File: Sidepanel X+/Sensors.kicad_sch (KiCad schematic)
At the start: 8 parts, among them IC1 TMP112AQDRLRQ1, U1 GUVA-C32SM

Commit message: fix for the issues: #19, #18 moved some components from the edge away to avoid collisions with the new structure
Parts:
- U1: footprint Package_SO:SO-4_4.4x3.6mm_P2.54mm -> STS_UV:OLGA 2mm x 2,3mm
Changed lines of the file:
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@@
     (property "Reference" "U1" (id 0) (at 60.96 34.29 0))
     (property "Value" "GUVA-C32SM" (id 1) (at 60.96 36.83 0))
-    (property "Footprint" "Package_SO:SO-4_4.4x3.6mm_P2.54mm" (id 2) (at 60.96 45.72 0)
+    (property "Footprint" "STS_UV:OLGA 2mm x 2,3mm" (id 2) (at 60.96 45.72 0)
       (effects (font (size 1.27 1.27)) hide)
     )

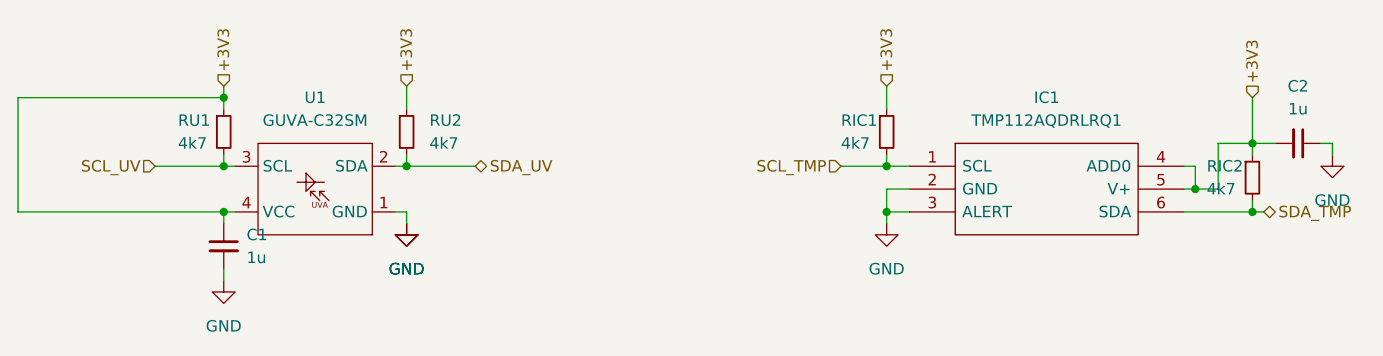
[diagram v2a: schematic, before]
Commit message: Changed the layout of all the sidepanel PCBs to mitigate the problems that arised from the bad previous design.
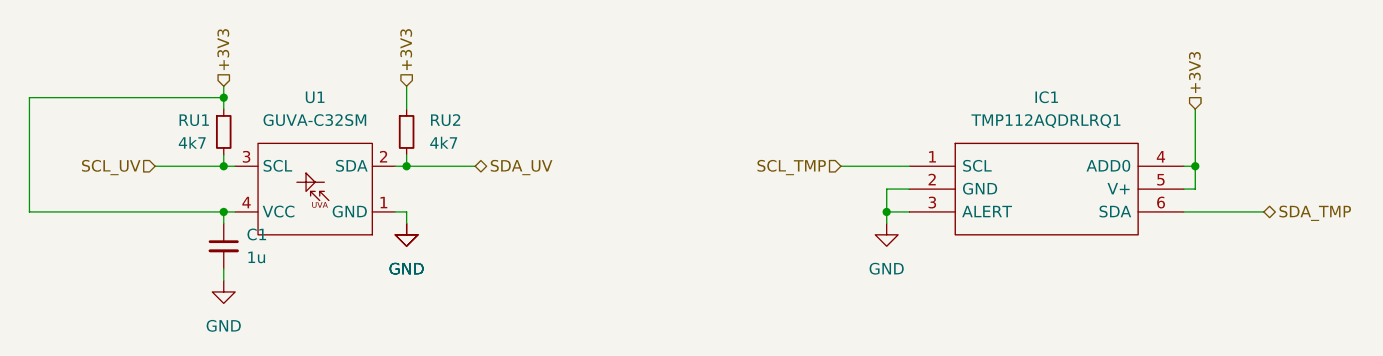
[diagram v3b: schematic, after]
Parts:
- removed C2: 1u, Capacitor_SMD:C_0603_1608Metric, symbol Device:C_Small
- removed RIC1, RIC2: 4k7, Resistor_SMD:R_0603_1608Metric, symbol Device:R_Small
- U1: footprint STS_UV:OLGA 2mm x 2,3mm -> STS_UV:OLGA

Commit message: Added a  separate ground for the EDU  sensors and did  some small changes for ordering.
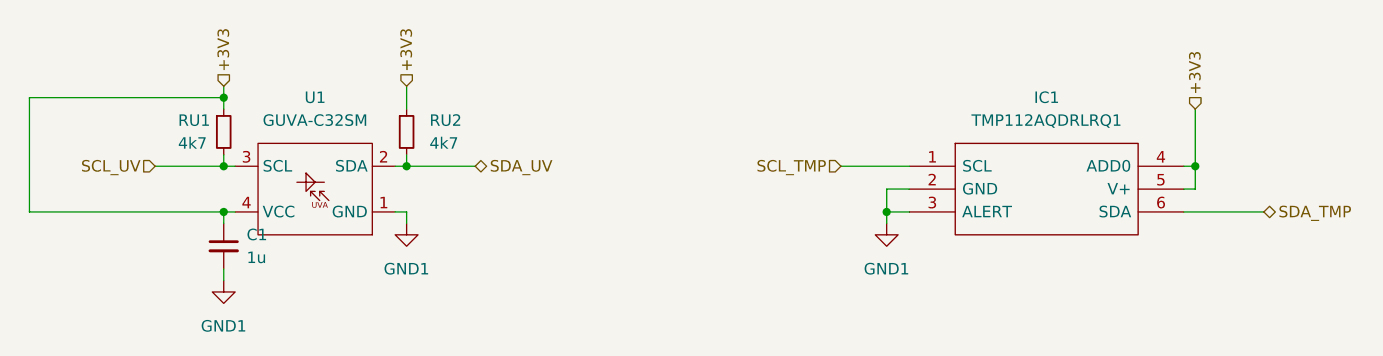
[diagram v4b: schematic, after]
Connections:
- net GND renamed GND1
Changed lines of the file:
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@@
     (effects (font (size 1.27 1.27)) (justify right))
   )
-  (symbol (lib_id "power:GND") (at 71.12 48.26 0) (unit 1)
-    (in_bom yes) (on_board yes) (dnp no) (fields_autoplaced)
-    (property "Reference" "#PWR03" (at 71.12 54.61 0)
-      (effects (font (size 1.27 1.27)) hide)
-    )
-    (property "Value" "GND" (at 71.12 53.34 0)
-      (effects (font (size 1.27 1.27)))
-    )
-    (property "Footprint" "" (at 71.12 48.26 0)
-      (effects (font (size 1.27 1.27)) hide)
-    )
-    (property "Datasheet" "" (at 71.12 48.26 0)
-      (effects (font (size 1.27 1.27)) hide)
-    )
-    (pin "1")
-    (instances
-      (project "STS1_SIDEPANEL"
-        (path "/e63e39d7-6ac0-4ffd-8aa3-1841a4541b55/9d03bb93-a9aa-424f-bd25-022f173efd1d"
-          (reference "#PWR03") (unit 1)
-        )
-      )
-    )
-  )
-  (symbol (lib_id "power:GND") (at 124.46 48.26 0) (unit 1)
-    (in_bom yes) (on_board yes) (dnp no) (fields_autoplaced)
-    (property "Reference" "#PWR0101" (at 124.46 54.61 0)
-      (effects (font (size 1.27 1.27)) hide)
-    )
-    (property "Value" "GND" (at 124.46 53.34 0)
-      (effects (font (size 1.27 1.27)))
-    )
-    (property "Footprint" "" (at 124.46 48.26 0)
-      (effects (font (size 1.27 1.27)) hide)
-    )
-    (property "Datasheet" "" (at 124.46 48.26 0)
-      (effects (font (size 1.27 1.27)) hide)
-    )
-    (pin "1")
-    (instances
-      (project "STS1_SIDEPANEL"
-        (path "/e63e39d7-6ac0-4ffd-8aa3-1841a4541b55/9d03bb93-a9aa-424f-bd25-022f173efd1d"
-          (reference "#PWR0101") (unit 1)
-        )
-      )
-    )
-  )
-  (symbol (lib_id "power:GND") (at 71.12 48.26 0) (unit 1)
-    (in_bom yes) (on_board yes) (dnp no) (fields_autoplaced)
-    (property "Reference" "#PWR04" (at 71.12 54.61 0)
-      (effects (font (size 1.27 1.27)) hide)
-    )
-    (property "Value" "GND" (at 71.12 53.34 0)
-      (effects (font (size 1.27 1.27)))
-    )
-    (property "Footprint" "" (at 71.12 48.26 0)
-      (effects (font (size 1.27 1.27)) hide)
-    )
-    (property "Datasheet" "" (at 71.12 48.26 0)
-      (effects (font (size 1.27 1.27)) hide)
-    )
-    (pin "1")
-    (instances
-      (project "STS1_SIDEPANEL"
-        (path "/e63e39d7-6ac0-4ffd-8aa3-1841a4541b55/9d03bb93-a9aa-424f-bd25-022f173efd1d"
-          (reference "#PWR04") (unit 1)
+  (symbol (lib_id "power:GND1") (at 50.8 54.61 0) (unit 1)
+    (in_bom yes) (on_board yes) (dnp no) (fields_autoplaced)
+    (property "Reference" "#PWR02" (at 50.8 60.96 0)
+      (effects (font (size 1.27 1.27)) hide)
+    )
+    (property "Value" "GND1" (at 50.8 59.69 0)
+      (effects (font (size 1.27 1.27)))
+    )
+    (property "Footprint" "" (at 50.8 54.61 0)
+      (effects (font (size 1.27 1.27)) hide)
+    )
+    (property "Datasheet" "" (at 50.8 54.61 0)
+      (effects (font (size 1.27 1.27)) hide)
+    )
+    (pin "1")
+    (instances
+      (project "STS1_SIDEPANEL"
+        (path "/e63e39d7-6ac0-4ffd-8aa3-1841a4541b55/9d03bb93-a9aa-424f-bd25-022f173efd1d"
+          (reference "#PWR02") (unit 1)
         )
       )
@@
         (path "/e63e39d7-6ac0-4ffd-8aa3-1841a4541b55/9d03bb93-a9aa-424f-bd25-022f173efd1d"
           (reference "U1") (unit 1)
+        )
+      )
+    )
+  )
+  (symbol (lib_id "power:GND1") (at 124.46 48.26 0) (unit 1)
+    (in_bom yes) (on_board yes) (dnp no) (fields_autoplaced)
+    (property "Reference" "#PWR04" (at 124.46 54.61 0)
+      (effects (font (size 1.27 1.27)) hide)
+    )
+    (property "Value" "GND1" (at 124.46 53.34 0)
+      (effects (font (size 1.27 1.27)))
+    )
+    (property "Footprint" "" (at 124.46 48.26 0)
+      (effects (font (size 1.27 1.27)) hide)
+    )
+    (property "Datasheet" "" (at 124.46 48.26 0)
+      (effects (font (size 1.27 1.27)) hide)
+    )
+    (pin "1")
+    (instances
+      (project "STS1_SIDEPANEL"
+        (path "/e63e39d7-6ac0-4ffd-8aa3-1841a4541b55/9d03bb93-a9aa-424f-bd25-022f173efd1d"
+          (reference "#PWR04") (unit 1)
+        )
+      )
+    )
+  )
+  (symbol (lib_id "power:GND1") (at 71.12 48.26 0) (unit 1)
+    (in_bom yes) (on_board yes) (dnp no) (fields_autoplaced)
+    (property "Reference" "#PWR03" (at 71.12 54.61 0)
+      (effects (font (size 1.27 1.27)) hide)
+    )
+    (property "Value" "GND1" (at 71.12 53.34 0)
+      (effects (font (size 1.27 1.27)))
+    )
+    (property "Footprint" "" (at 71.12 48.26 0)
+      (effects (font (size 1.27 1.27)) hide)
+    )
+    (property "Datasheet" "" (at 71.12 48.26 0)
+      (effects (font (size 1.27 1.27)) hide)
+    )
+    (pin "1")
+    (instances
+      (project "STS1_SIDEPANEL"
+        (path "/e63e39d7-6ac0-4ffd-8aa3-1841a4541b55/9d03bb93-a9aa-424f-bd25-022f173efd1d"
+          (reference "#PWR03") (unit 1)
         )
       )
@@
         )
       )
-    )
-  )
-  (symbol (lib_id "power:GND") (at 50.8 54.61 0) (unit 1)
-    (in_bom yes) (on_board yes) (dnp no) (fields_autoplaced)
-    (property "Reference" "#PWR02" (at 50.8 60.96 0)
-      (effects (font (size 1.27 1.27)) hide)
-    )
-    (property "Value" "GND" (at 50.8 59.69 0)
-      (effects (font (size 1.27 1.27)))
-    )
-    (property "Footprint" "" (at 50.8 54.61 0)
-      (effects (font (size 1.27 1.27)) hide)
-    )
-    (property "Datasheet" "" (at 50.8 54.61 0)
-      (effects (font (size 1.27 1.27)) hide)
-    )
-    (pin "1")
-    (instances
-      (project "STS1_SIDEPANEL"
-        (path "/e63e39d7-6ac0-4ffd-8aa3-1841a4541b55/9d03bb93-a9aa-424f-bd25-022f173efd1d"
-          (reference "#PWR02") (unit 1)
-        )
-      )
